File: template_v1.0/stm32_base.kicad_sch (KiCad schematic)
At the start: 45 parts, among them J1 Network Connector, J2 STDC14, SW1 SW_Push, U1 TSR1-2450E, U2 STM32G474RBT6, U3 TJA1042T-3, Y1 8MHz

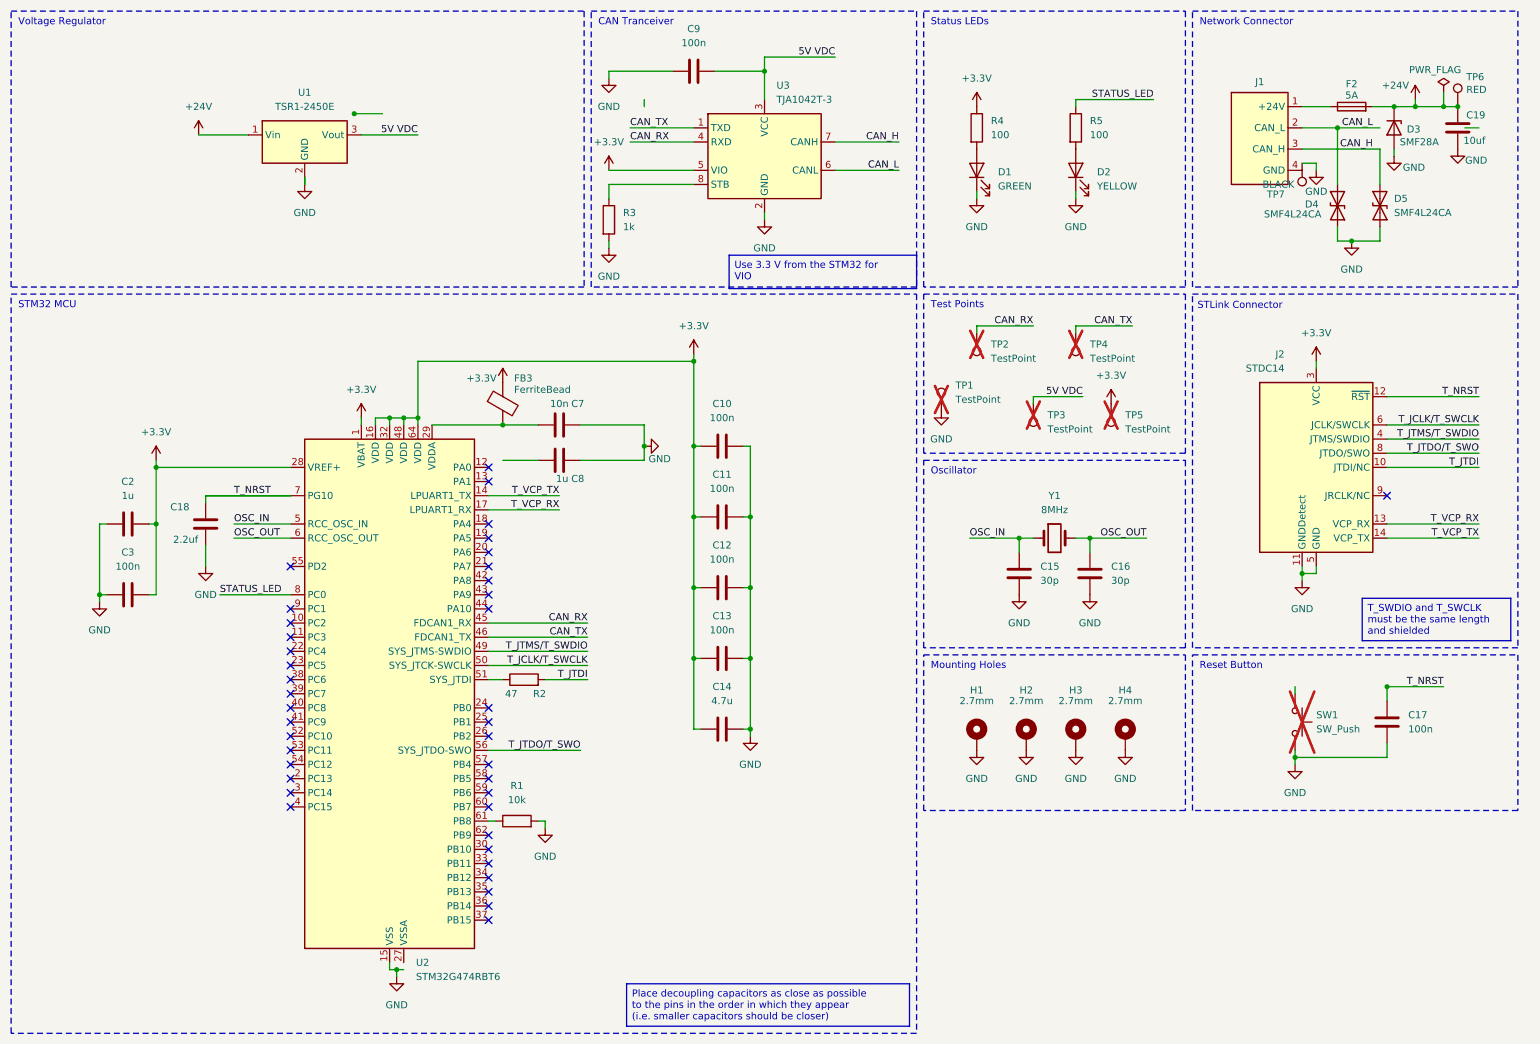
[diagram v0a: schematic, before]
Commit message: Exo-template-pcb : footprints library resolve
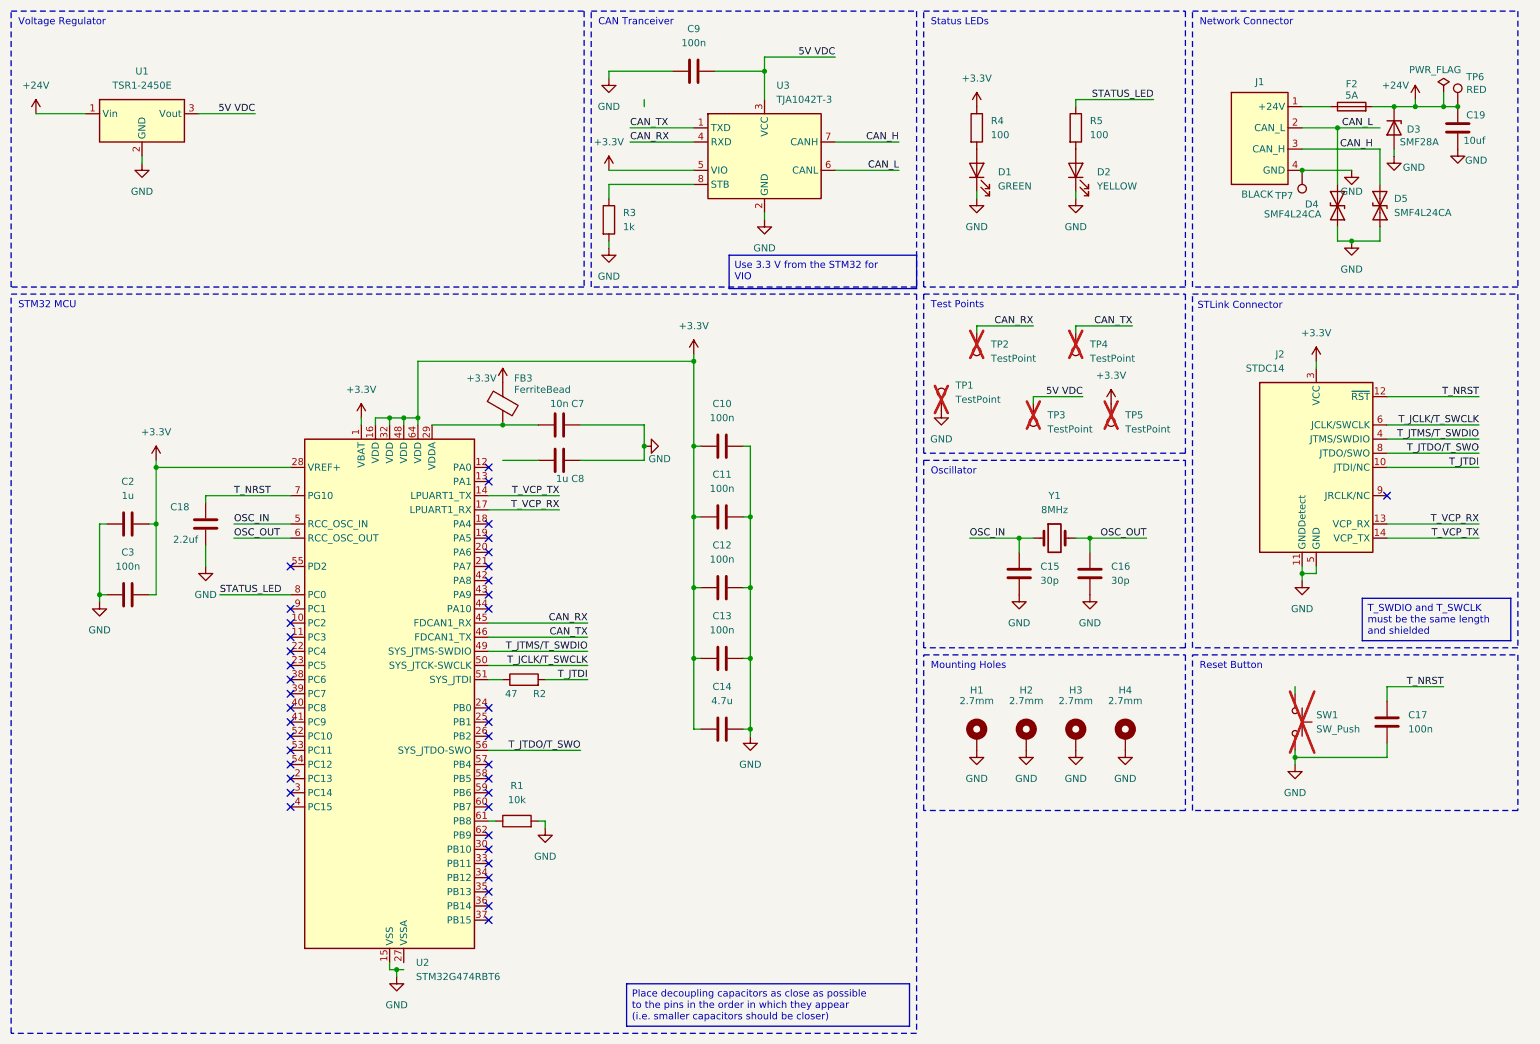
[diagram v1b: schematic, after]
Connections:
- net GND: now also J1.4 (GND)
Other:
- moved on the sheet: TP7, U1
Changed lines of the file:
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@@
 	)
 	(junction
+		(at 245.11 41.91)
+		(diameter 0)
+		(color 0 0 0 0)
+	)
+	(junction
 		(at 81.28 86.36)
 		(diameter 0)
@@
 	)
 	(junction
-		(at 260.35 134.62)
-		(diameter 0)
-		(color 0 0 0 0)
-	)
-	(junction
-		(at 74.93 31.75)
-		(diameter 0)
-		(color 0 0 0 0)
-	)
-	(junction
 		(at 135.89 91.44)
 		(diameter 0)
@@
 	(wire
 		(pts
-			(xy 76.2 35.56) (xy 86.36 35.56)
+			(xy 46.99 31.75) (xy 57.15 31.75)
 		)
 		(stroke
@@
 	(wire
 		(pts
-			(xy 247.65 40.64) (xy 247.65 41.91)
-		)
-		(stroke
-			(width 0)
-			(type default)
-		)
-	)
-	(wire
-		(pts
 			(xy 101.6 93.98) (xy 107.95 93.98)
 		)
@@
 	(wire
 		(pts
-			(xy 66.04 43.18) (xy 66.04 44.45)
-		)
-		(stroke
-			(width 0)
-			(type default)
-		)
-	)
-	(wire
-		(pts
-			(xy 66.04 43.18) (xy 66.04 44.45)
+			(xy 36.83 39.37) (xy 36.83 40.64)
 		)
 		(stroke
@@
 	(wire
 		(pts
-			(xy 48.26 100.33) (xy 63.5 100.33)
-		)
-		(stroke
-			(width 0)
-			(type default)
-		)
-	)
-	(wire
-		(pts
-			(xy 245.11 40.64) (xy 247.65 40.64)
+			(xy 245.11 41.91) (xy 254 41.91)
 		)
 		(stroke
@@
 	(wire
 		(pts
-			(xy 74.93 31.75) (xy 80.01 31.75)
-		)
-		(stroke
-			(width 0)
-			(type default)
-		)
-	)
-	(wire
-		(pts
 			(xy 29.21 105.41) (xy 29.21 118.11)
 		)
@@
 	(wire
 		(pts
-			(xy 46.99 35.56) (xy 55.88 35.56)
+			(xy 17.78 31.75) (xy 26.67 31.75)
 		)
 		(stroke
@@
 	(wire
 		(pts
-			(xy 276.86 34.29) (xy 274.32 34.29)
-		)
-		(stroke
-			(width 0)
-			(type default)
-		)
-	)
-	(wire
-		(pts
 			(xy 135.89 142.24) (xy 137.16 142.24)
 		)
@@
 	)
 	(label "5V VDC"
-		(at 86.36 35.56 180)
+		(at 57.15 31.75 180)
 		(effects
 			(font
@@
 	(symbol
 		(lib_id "power:GND")
-		(at 66.04 44.45 0)
+		(at 36.83 40.64 0)
 		(unit 1)
 		(body_style 1)
@@
 		(fields_autoplaced yes)
 		(property "Reference" "#PWR01"
-			(at 66.04 50.8 0)
+			(at 36.83 46.99 0)
 			(hide yes)
 			(show_name no)
@@
 		)
 		(property "Value" "GND"
-			(at 66.04 49.53 0)
+			(at 36.83 45.72 0)
 			(show_name no)
 			(do_not_autoplace no)
@@
 		)
 		(property "Footprint" "Converter_DCDC:Converter_DCDC_TRACO_TSR1-xxxxE_THT"
-			(at 66.04 44.45 0)
+			(at 36.83 40.64 0)
 			(hide yes)
 			(show_name no)
@@
 		)
 		(property "Datasheet" ""
-			(at 66.04 44.45 0)
+			(at 36.83 40.64 0)
 			(hide yes)
 			(show_name no)
@@
 		)
 		(property "Description" "Power symbol creates a global label with name \"GND\" , ground"
-			(at 66.04 44.45 0)
+			(at 36.83 40.64 0)
 			(hide yes)
 			(show_name no)
@@
 	(symbol
 		(lib_id "Connector:TestPoint")
-		(at 245.11 40.64 180)
+		(at 245.11 41.91 180)
 		(unit 1)
 		(body_style 1)
@@
 		(dnp no)
 		(property "Reference" "TP7"
-			(at 238.76 46.228 0)
+			(at 240.284 46.482 0)
 			(show_name no)
 			(do_not_autoplace no)
@@
 		)
 		(property "Value" "BLACK"
-			(at 237.998 44.45 0)
+			(at 234.188 46.228 0)
 			(show_name no)
 			(do_not_autoplace no)
@@
 		)
 		(property "Footprint" ""
-			(at 240.03 40.64 0)
+			(at 240.03 41.91 0)
 			(hide yes)
 			(show_name no)
@@
 		)
 		(property "Datasheet" ""
-			(at 240.03 40.64 0)
+			(at 240.03 41.91 0)
 			(hide yes)
 			(show_name no)
@@
 		)
 		(property "Description" "test point"
-			(at 245.11 40.64 0)
+			(at 245.11 41.91 0)
 			(hide yes)
 			(show_name no)
@@
 			)
 		)
-		(pin "3"
-		)
 		(pin "1"
 		)
@@
 	(symbol
 		(lib_id "Converter_DCDC:TSR1-2450E")
-		(at 66.04 38.1 0)
+		(at 36.83 34.29 0)
 		(unit 1)
 		(body_style 1)
@@
 		(fields_autoplaced yes)
 		(property "Reference" "U1"
-			(at 66.04 27.94 0)
+			(at 36.83 24.13 0)
 			(show_name no)
 			(do_not_autoplace no)
@@
 		)
 		(property "Value" "TSR1-2450E"
-			(at 66.04 30.48 0)
+			(at 36.83 26.67 0)
 			(show_name no)
 			(do_not_autoplace no)
@@
 		)
 		(property "Footprint" "Converter_DCDC:Converter_DCDC_TRACO_TSR1-xxxxE_THT"
-			(at 66.04 44.45 0)
+			(at 36.83 40.64 0)
 			(hide yes)
 			(show_name no)
@@
 		)
 		(property "Datasheet" "https://www.tracopower.com/products/tsr1e.pdf"
-			(at 66.04 41.91 0)
+			(at 36.83 38.1 0)
 			(hide yes)
 			(show_name no)
@@
 		)
 		(property "Description" "1A step-down regulator, fixed 5V output voltage, 7-36V input voltage, TO-220 compatible LM78xx replacement"
-			(at 66.04 38.1 0)
+			(at 36.83 34.29 0)
 			(hide yes)
 			(show_name no)
@@
 	(symbol
 		(lib_id "power:+24V")
-		(at 46.99 35.56 0)
+		(at 17.78 31.75 0)
 		(unit 1)
 		(body_style 1)
@@
 		(fields_autoplaced yes)
 		(property "Reference" "#PWR04"
-			(at 46.99 39.37 0)
+			(at 17.78 35.56 0)
 			(hide yes)
 			(show_name no)
@@
 		)
 		(property "Value" "+24V"
-			(at 46.99 30.48 0)
+			(at 17.78 26.67 0)
 			(show_name no)
 			(do_not_autoplace no)
@@
 		)
 		(property "Footprint" "Package_SO:SOIC-8_3.9x4.9mm_P1.27mm"
-			(at 46.99 35.56 0)
+			(at 17.78 31.75 0)
 			(hide yes)
 			(show_name no)
@@
 		)
 		(property "Datasheet" ""
-			(at 46.99 35.56 0)
+			(at 17.78 31.75 0)
 			(hide yes)
 			(show_name no)
@@
 		)
 		(property "Description" "Power symbol creates a global label with name \"+24V\""
-			(at 46.99 35.56 0)
+			(at 17.78 31.75 0)
 			(hide yes)
 			(show_name no)
@@
 	(symbol
 		(lib_id "power:GND")
-		(at 247.65 41.91 0)
+		(at 254 41.91 0)
 		(unit 1)
 		(body_style 1)
@@
 		(dnp no)
 		(property "Reference" "#PWR033"
-			(at 247.65 48.26 0)
+			(at 254 48.26 0)
 			(hide yes)
 			(show_name no)
@@
 		)
 		(property "Value" "GND"
-			(at 247.65 45.72 0)
+			(at 254 45.72 0)
 			(show_name no)
 			(do_not_autoplace no)
@@
 		)
 		(property "Footprint" ""
-			(at 247.65 41.91 0)
+			(at 254 41.91 0)
 			(hide yes)
 			(show_name no)
@@
 		)
 		(property "Datasheet" ""
-			(at 247.65 41.91 0)
+			(at 254 41.91 0)
 			(hide yes)
 			(show_name no)
@@
 		)
 		(property "Description" "Power symbol creates a global label with name \"GND\" , ground"
-			(at 247.65 41.91 0)
+			(at 254 41.91 0)
 			(hide yes)
 			(show_name no)

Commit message: Exo-template-pcb : Resolve all issues - add 3.3V regulator - add jlcpcb numbers
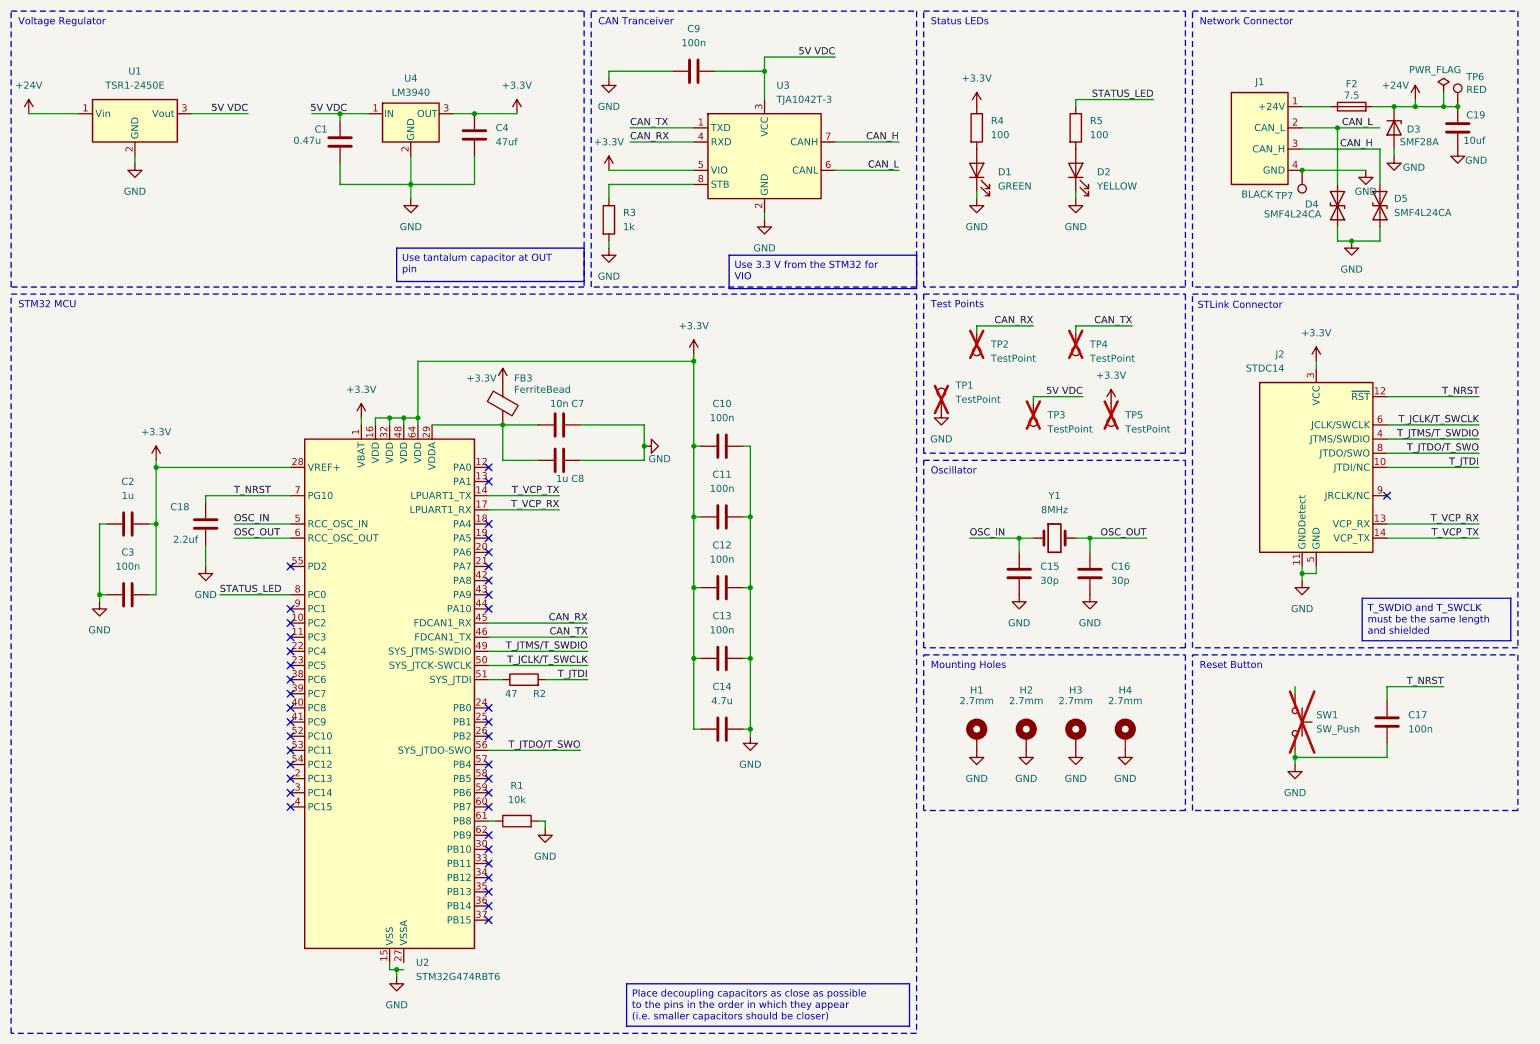
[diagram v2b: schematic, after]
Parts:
- added C1: 0.47u, Capacitor_SMD:C_0201_0603Metric, symbol Device:C
- added C4: 47uf, Capacitor_Tantalum_SMD:CP_EIA-3216-10_Kemet-I, symbol Device:C
- added U4: LM3940, Package_TO_SOT_THT:TO-220-3_Vertical, symbol Exocet:LM3940
- F2: value 5A -> 7.5
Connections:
- net +3.3V: now also C4.1, U4.3 (OUT)
- net 5V VDC: now also C1.1, U4.1 (IN)
- net GND: now also C1.2, C4.2, U4.2 (GND)
- net at C7.1, FB3.2, U2.29 (VDDA): now also C8.1
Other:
- moved on the sheet: U1
